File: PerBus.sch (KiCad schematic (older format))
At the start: 6 parts, among them J1 CONN-10018783-10202TLF-PCIEx8, J2 CONN-10018783-10202TLF-PCIEx8, J3 CONN-10018783-10202TLF-PCIEx8, J4 CONN-10018783-10202TLF-PCIEx8, J5 CONN-10018783-10202TLF-PCIEx8, J6 CONN-10018783-10202TLF-PCIEx8

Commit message: Upgrade FPGA size, re-route SDRAM
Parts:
- removed J5, J6: CONN-10018783-10202TLF-PCIEx8, conn-fci:CONN-10018783-10202TLF-PCIEx8-FCI, symbol CONN-10018783-10202TLF-PCIEx8
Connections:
- net labels removed: PAR_~PRSNT4, PAR_~PRSNT5, SER_~PRSNT4, SER_~PRSNT5, ~IRQ4, ~IRQ5, ~SS4, ~SS5
- wire segments 595 -> 399
- no-connect marks 18 -> 12

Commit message: Begin implementing PCI
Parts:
- removed J1, J2, J3, J4: CONN-10018783-10202TLF-PCIEx8, conn-fci:CONN-10018783-10202TLF-PCIEx8-FCI, symbol CONN-10018783-10202TLF-PCIEx8
- added PCI0, PCI1, PCI2, PCI3: CONN-5145154-1-PCI, conn-te:5145154-1, symbol CONN-5145154-1-PCI
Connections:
- net labels added: PCI_ACK64#, PCI_AD00, PCI_AD01, PCI_AD02, PCI_AD03, PCI_AD04, PCI_AD05, PCI_AD06, PCI_AD07, PCI_AD08, PCI_AD09, PCI_AD10, PCI_AD11, PCI_AD12, PCI_AD13, PCI_AD14, PCI_AD15, PCI_AD16, PCI_AD17, PCI_AD18, PCI_AD19, PCI_AD20, PCI_AD21, PCI_AD22, PCI_AD23, PCI_AD24, PCI_AD25, PCI_AD26, PCI_AD27, PCI_AD28, PCI_AD29, PCI_AD30, PCI_AD31, PCI_CBE#0, PCI_CBE#1, PCI_CBE#2, PCI_CBE#3, PCI_CLK, PCI_DEVSEL#, PCI_FRAME#, PCI_GNT#0, PCI_IDSEL0, PCI_INTA#, PCI_INTB#, PCI_INTC#, PCI_INTD#, PCI_IRDY#, PCI_LOCK#, PCI_M66EN, PCI_N12, PCI_P12, PCI_P3V3, PCI_P3V3AUX, PCI_P5, PCI_PAR, PCI_PERR#, PCI_PME#, PCI_PRSNT1#, PCI_PRSNT2#, PCI_REQ#0, PCI_REQ64#, PCI_RST#, PCI_SERR#, PCI_SMBCLK, PCI_SMBDAT, PCI_STOP#, PCI_TCK, PCI_TDI, PCI_TDO, PCI_TMS, PCI_TRDY#, PCI_TRST#, PCI_VIO, PCI_XCAP
- net labels removed: +12, +3.3, +3.3SB, CD[0..31], CLK, D0, D1, D10, D11, D12, D13, D14, D15, D16, D17, D18, D19, D2, D20, D21, D22, D23, D24, D25, D26, D27, D28, D29, D3, D30, D31, D4, D5, D6, D7, D8, D9, D[0..31], PAR_~PRSNT0, PAR_~PRSNT1, PAR_~PRSNT2, PAR_~PRSNT3, R/~W, SER_CLK, SER_MISO, SER_MOSI, SER_~PRSNT0, SER_~PRSNT1, SER_~PRSNT2, SER_~PRSNT3, SER_~SS~_0, ~ADH, ~ADL, ~IRQ0, ~IRQ1, ~IRQ2, ~IRQ3, ~PERST, ~SS0, ~SS1, ~SS2, ~SS3, ~SS[0..5]
- wire segments 399 -> 464
- no-connect marks 12 -> 16

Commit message: PCI bus decoupling
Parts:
- added C35, C39, C43, C47, C51, C52, C53, C54: 47u, pth-passive:C-ALUM-6.3mm, symbol C-ALUM-6.3mm
- added C36, C37, C38, C40, C41, C42, C44, C45, C46, C48, C49, C50: 220u, pth-passive:C-ALUM-6.3mm, symbol C-ALUM-6.3mm
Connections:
- net GND: now also C35.2, C36.2, C37.2, C38.2, C39.2, C40.2, C41.2, C42.2, C43.2, C44.2, C45.2, C46.2, C47.2, C48.2, C49.2, C50.2, C51.1, C52.1, C53.1, C54.1
- net PCI_N12: now also C51.2, C52.2, C53.2, C54.2
- net PCI_P12: now also C35.1, C39.1, C43.1, C47.1
- net PCI_P3V3: now also C38.1, C42.1, C46.1, C50.1
- net PCI_P5: now also C36.1, C40.1, C44.1, C48.1
- net PCI_VIO: now also C37.1, C41.1, C45.1, C49.1
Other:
- note added: "5V: 25W 5A\n3.3V: 25W 7.6A\n12V: 6W 500mA\n-12V: 1.2W 100mA\n3v3aux: 1.3W 375mA\nVio: 5W 1.5A"

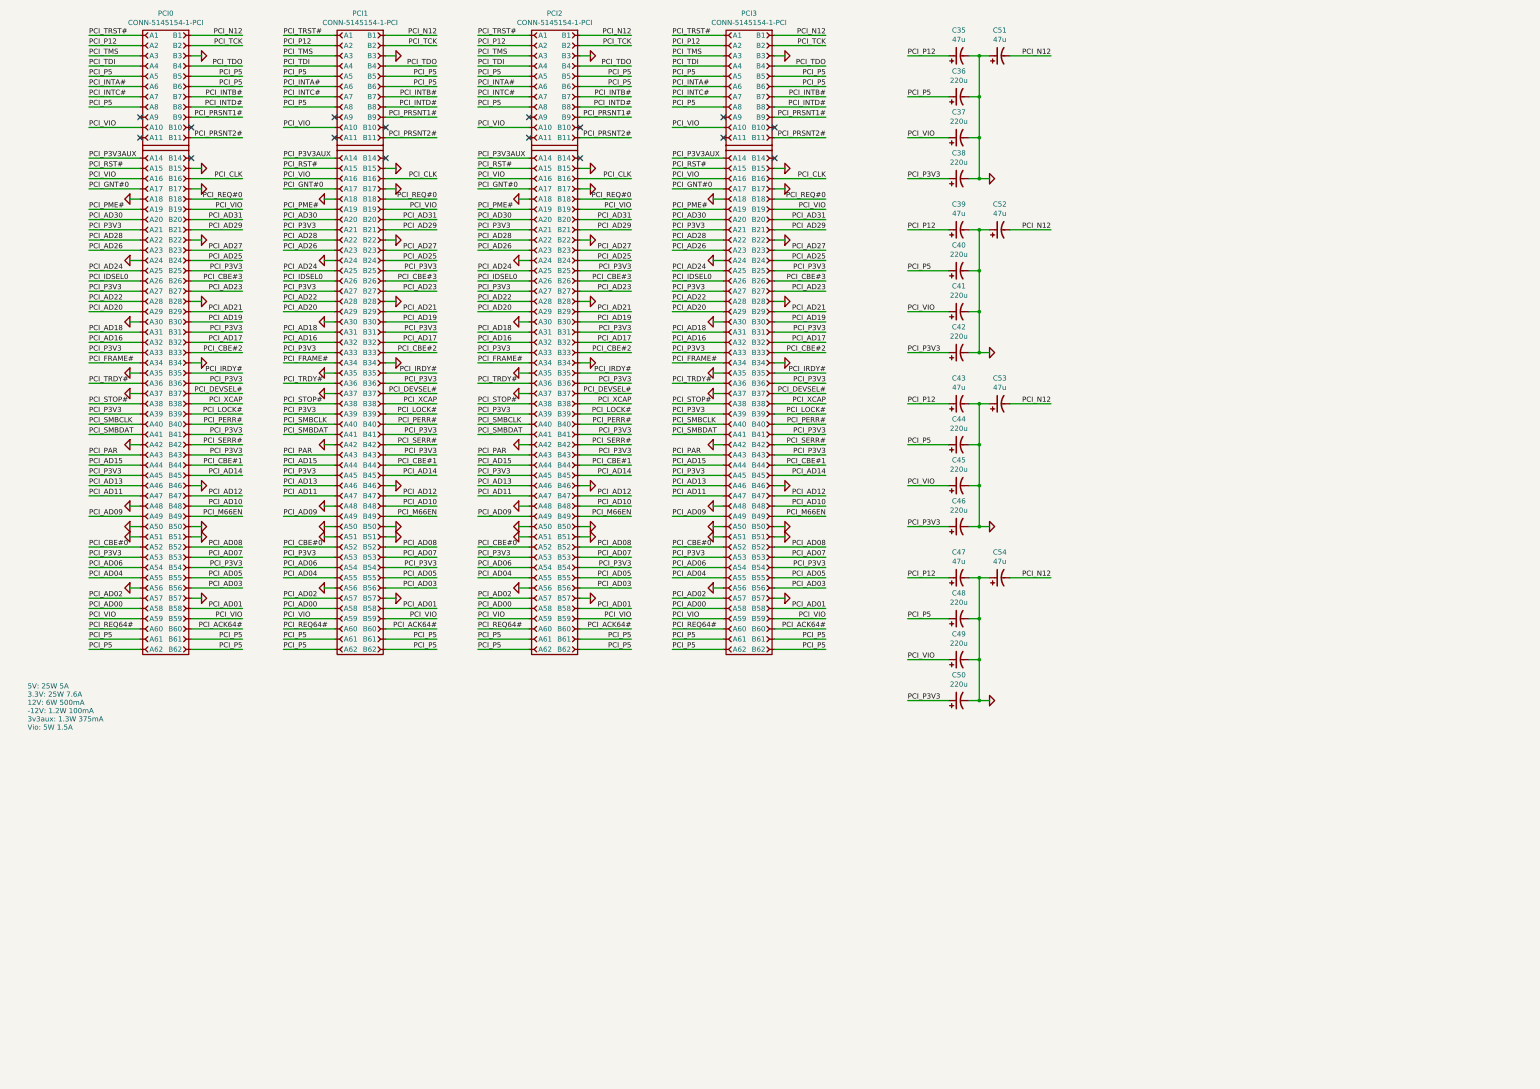
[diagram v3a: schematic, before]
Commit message: Continue routing PCI
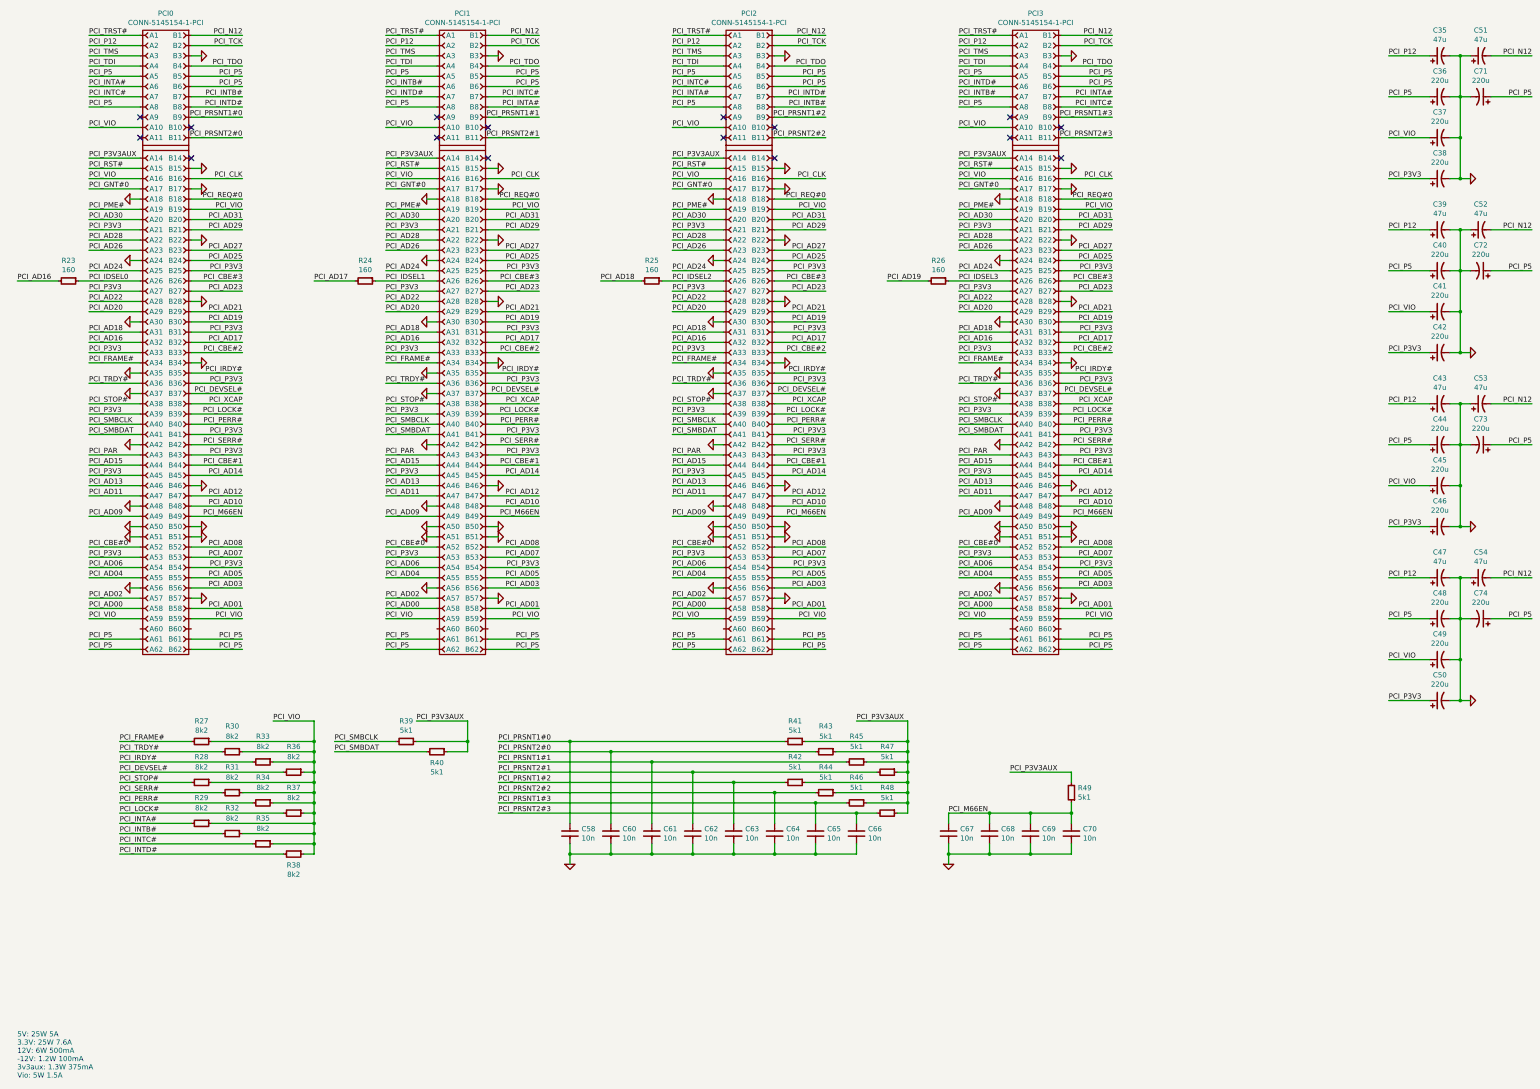
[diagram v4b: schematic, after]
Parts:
- added C58, C60, C61, C62, C63, C64, C65, C66, C67, C68, C69, C70: 10n, IPC7351-Nominal:CAPC1005X55, symbol C-0402
- added C71, C72, C73, C74: 220u, pth-passive:C-ALUM-6.3mm, symbol C-ALUM-6.3mm
- added R23, R24, R25, R26: 160, IPC7351-Nominal:RESC1608X50, symbol R-0603
- added R27, R28, R29, R30, R31, R32, R33, R34, R35, R36, R37, R38: 8k2, IPC7351-Nominal:RESC1608X50, symbol R-0603
- added R39, R40, R41, R42, R43, R44, R45, R46, R47, R48, R49: 5k1, IPC7351-Nominal:RESC1608X50, symbol R-0603
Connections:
- net GND: now also C58.2, C60.2, C61.2, C62.2, C63.2, C64.2, C65.2, C66.2, C67.2, C68.2, C69.2, C70.2, C71.2, C72.2, C73.2, C74.2
- net PCI_AD16: now also R23.2
- net PCI_AD17: now also R24.2
- net PCI_AD18: now also R25.2
- net PCI_AD19: now also R26.2
- net PCI_DEVSEL#: now also R36.2
- net PCI_FRAME#: now also R27.2
- net PCI_IDSEL0: now also R23.1; no longer PCI1.A26, PCI2.A26, PCI3.A26
- net PCI_INTA#: now also PCI1.B8, PCI2.A7, PCI3.B7, R29.2; no longer PCI1.A6, PCI2.A6, PCI3.A6
- net PCI_INTB#: now also PCI1.A6, PCI2.B8, PCI3.A7, R32.2; no longer PCI1.B7, PCI2.B7, PCI3.B7
- net PCI_INTC#: now also PCI1.B7, PCI2.A6, PCI3.B8, R35.2; no longer PCI1.A7, PCI2.A7, PCI3.A7
- net PCI_INTD#: now also PCI1.A7, PCI2.B7, PCI3.A6, R38.2; no longer PCI1.B8, PCI2.B8, PCI3.B8
- net PCI_IRDY#: now also R33.2
- net PCI_LOCK#: now also R37.2
- net PCI_M66EN: now also C67.1, C68.1, C69.1, C70.1, R49.1
- net PCI_P3V3AUX: now also R39.1, R40.1, R41.1, R42.1, R43.1, R44.1, R45.1, R46.1, R47.1, R48.1, R49.2
- net PCI_P5: now also C71.1, C72.1, C73.1, C74.1
- net PCI_PERR#: now also R34.2
- net PCI_SERR#: now also R31.2
- net PCI_SMBCLK: now also R39.2
- net PCI_SMBDAT: now also R40.2
- net PCI_STOP#: now also R28.2
- net PCI_TRDY#: now also R30.2
- net PCI_VIO: now also R27.1, R28.1, R29.1, R30.1, R31.1, R32.1, R33.1, R34.1, R35.1, R36.1, R37.1, R38.1
- removed net PCI_ACK64#: PCI0.B60, PCI1.B60, PCI2.B60, PCI3.B60
- removed net PCI_PRSNT1#: PCI0.B9, PCI1.B9, PCI2.B9, PCI3.B9
- removed net PCI_PRSNT2#: PCI0.B11, PCI1.B11, PCI2.B11, PCI3.B11
- removed net PCI_REQ64#: PCI0.A60, PCI1.A60, PCI2.A60, PCI3.A60
- new net PCI_IDSEL1: PCI1.A26, R24.1
- new net PCI_IDSEL2: PCI2.A26, R25.1
- new net PCI_IDSEL3: PCI3.A26, R26.1
- new net PCI_PRSNT1#0: C58.1, PCI0.B9, R41.2
- new net PCI_PRSNT1#1: C61.1, PCI1.B9, R45.2
- new net PCI_PRSNT1#2: C63.1, PCI2.B9, R42.2
- new net PCI_PRSNT1#3: C65.1, PCI3.B9, R46.2
- new net PCI_PRSNT2#0: C60.1, PCI0.B11, R43.2
- new net PCI_PRSNT2#1: C62.1, PCI1.B11, R47.2
- new net PCI_PRSNT2#2: C64.1, PCI2.B11, R44.2
- new net PCI_PRSNT2#3: C66.1, PCI3.B11, R48.2
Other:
- moved on the sheet: C35, C36, C37, C38, C39, C40, C41, C42, C43, C44, C45, C46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

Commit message: More PCI work
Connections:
- net PCI_XCAP is gone; now on net GND: PCI0.B38, PCI1.B38, PCI2.B38, PCI3.B38
